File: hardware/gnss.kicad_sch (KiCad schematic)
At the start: 3 parts, among them J1 RF2-04A-T-00-50-G, U2 NEO-M9N

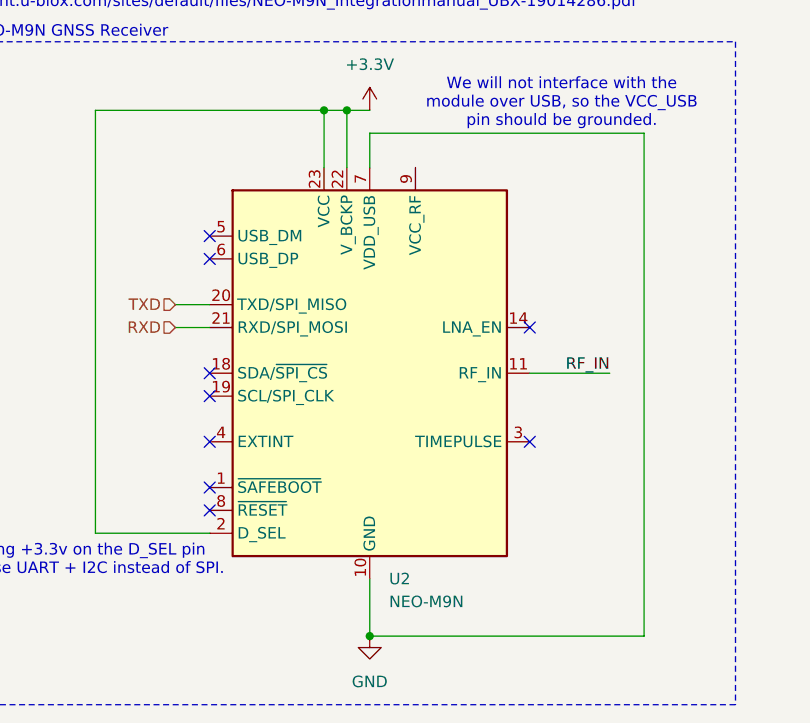
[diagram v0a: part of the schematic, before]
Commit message: begin stm32 implementation and remove battery charger for simplicity
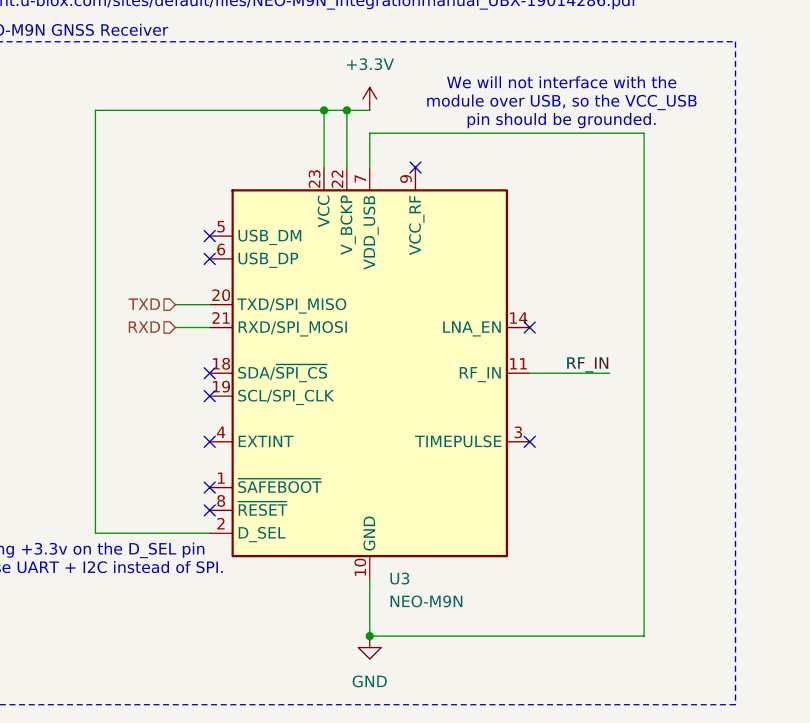
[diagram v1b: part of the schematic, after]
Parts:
- renumbered U2 to U3
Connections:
- no-connect marks 9 -> 10
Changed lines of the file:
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@@
+	)
+	(no_connect
+		(at 71.12 63.5)
 	)
 	(no_connect
@@
 		(dnp no)
 		(fields_autoplaced yes)
-		(property "Reference" "U2"
+		(property "Reference" "U3"
 			(at 68.1833 109.22 0)
 			(effects
@@
 			(project ""
 				(path "/34886a96-89cd-4fc5-ba47-006a1318e849/12b9aa31-f253-4d27-91dd-ffc7b984f697"
-					(reference "U2")
+					(reference "U3")
 					(unit 1)
 				)
@@
 		(dnp no)
 		(fields_autoplaced yes)
-		(property "Reference" "#PWR04"
+		(property "Reference" "#PWR0101"
 			(at 38.1 39.37 0)
 			(effects
@@
 			(project ""
 				(path "/34886a96-89cd-4fc5-ba47-006a1318e849/12b9aa31-f253-4d27-91dd-ffc7b984f697"
-					(reference "#PWR04")
+					(reference "#PWR0101")
 					(unit 1)
 				)
@@
 		(dnp no)
 		(fields_autoplaced yes)
-		(property "Reference" "#PWR02"
+		(property "Reference" "#PWR0102"
 			(at 66.04 60.96 0)
 			(effects
@@
 			(project ""
 				(path "/34886a96-89cd-4fc5-ba47-006a1318e849/12b9aa31-f253-4d27-91dd-ffc7b984f697"
-					(reference "#PWR02")
+					(reference "#PWR0102")
 					(unit 1)
 				)
@@
 		(dnp no)
 		(fields_autoplaced yes)
-		(property "Reference" "#PWR01"
+		(property "Reference" "#PWR0103"
 			(at 66.04 121.92 0)
 			(effects
@@
 			(project ""
 				(path "/34886a96-89cd-4fc5-ba47-006a1318e849/12b9aa31-f253-4d27-91dd-ffc7b984f697"
-					(reference "#PWR01")
+					(reference "#PWR0103")
 					(unit 1)
 				)
